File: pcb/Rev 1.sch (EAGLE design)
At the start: 216 parts, among them J1 3220-10-0100-00, J2 10118194-0001LF, J3 B2B-PH-K-S(LF)(SN), Q1 MMBT3904,215MMBT3904,215, Q12 MMBT3904,215MMBT3904,215, Q13 MMBT3904,215MMBT3904,215, Q14 MMBT3904,215MMBT3904,215, Q15 MMBT3904,215MMBT3904,215, Q16 TEFT4300, Q17 TEFT4300, Q18 TEFT4300, Q19 TEFT4300, Q20 MMBT3904,215MMBT3904,215, Q21 MMBT3904,215MMBT3904,215, Q22 MMBT3904,215MMBT3904,215, Q23 MMBT3904,215MMBT3904,215, Q24 TEFT4300, Q25 TEFT4300, Q26 TEFT4300, Q27 TEFT4300, Q28 SI7157DP, Q29 SI7157DP, Q30 MMBT3906, Q31 MMBT3906, Q32 SI7157DP, Q33 MMBT3906, Q34 MMBT3906, U1 ATSAMD21G18A-MU, U10 DRV8871, U11 PCAL6416A, U12 MAX7315, U2 AP3441, U3 TPS61089, U4 BNO055, U5 MCP73811, U7 DRV8871, U8 DRV8871, U9 DRV8871

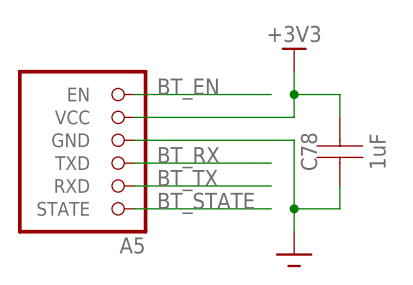
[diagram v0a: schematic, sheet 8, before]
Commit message: Switched power rail to HC-05
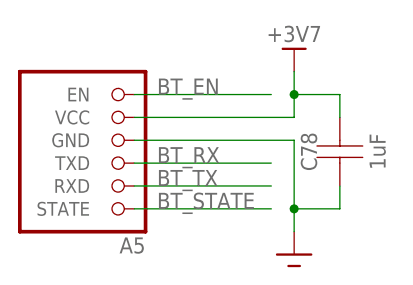
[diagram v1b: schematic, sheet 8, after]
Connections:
- net +3V3: no longer A5.VCC, C78.P$2
- net +3V7: now also A5.VCC, C78.P$2
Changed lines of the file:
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@@
 <part name="GND88" library="Micromouse 2020" deviceset="GND" device=""/>
 <part name="A5" library="Micromouse 2020" deviceset="HC-05" device=""/>
-<part name="P+69" library="Micromouse 2020" deviceset="+3V3" device=""/>
 <part name="GND91" library="Micromouse 2020" deviceset="GND" device=""/>
 <part name="C78" library="Micromouse 2020" deviceset="CAPACITOR" device="0603" package3d_urn="urn:adsk.eagle:package:16053670/1" value="1uF"/>
@@
 <part name="C48" library="Micromouse 2020" deviceset="CAPACITOR" device="0603" package3d_urn="urn:adsk.eagle:package:16053670/1" value="0.1uF"/>
 <part name="GND25" library="Micromouse 2020" deviceset="GND" device=""/>
+<part name="P+21" library="Micromouse 2020" deviceset="+3V7" device=""/>
 </parts>
 <sheets>
@@
 <attribute name="NAME" x="1.27" y="-10.795" size="1.778" layer="95" rot="R180"/>
 </instance>
-<instance part="P+69" gate="G$1" x="17.78" y="10.16" smashed="yes">
-<attribute name="VALUE" x="17.78" y="12.7" size="1.778" layer="96" rot="R180" align="bottom-center"/>
-</instance>
 <instance part="GND91" gate="1" x="17.78" y="-12.7" smashed="yes"/>
 <instance part="C78" gate="G$1" x="22.86" y="-5.08" smashed="yes" rot="R90">
@@
 <attribute name="VALUE" x="27.94" y="-1.27" size="1.778" layer="96" rot="R90" align="bottom-center"/>
 </instance>
+<instance part="P+21" gate="G$1" x="17.78" y="10.16" smashed="yes">
+<attribute name="VALUE" x="17.78" y="12.7" size="1.778" layer="96" rot="R180" align="bottom-center"/>
+</instance>
 </instances>
 <busses>
@@
 </segment>
 </net>
-<net name="+3V3" class="0">
+<net name="+3V7" class="0">
 <segment>
 <pinref part="A5" gate="G$1" pin="VCC"/>
 <wire x1="0" y1="2.54" x2="17.78" y2="2.54" width="0.1524" layer="91"/>
-<pinref part="P+69" gate="G$1" pin="+3V3"/>
 <wire x1="17.78" y1="2.54" x2="17.78" y2="5.08" width="0.1524" layer="91"/>
 <pinref part="C78" gate="G$1" pin="P$2"/>
@@
 <wire x1="22.86" y1="5.08" x2="17.78" y2="5.08" width="0.1524" layer="91"/>
 <junction x="17.78" y="5.08"/>
+<pinref part="P+21" gate="G$1" pin="+3V7"/>
 </segment>
 </net>

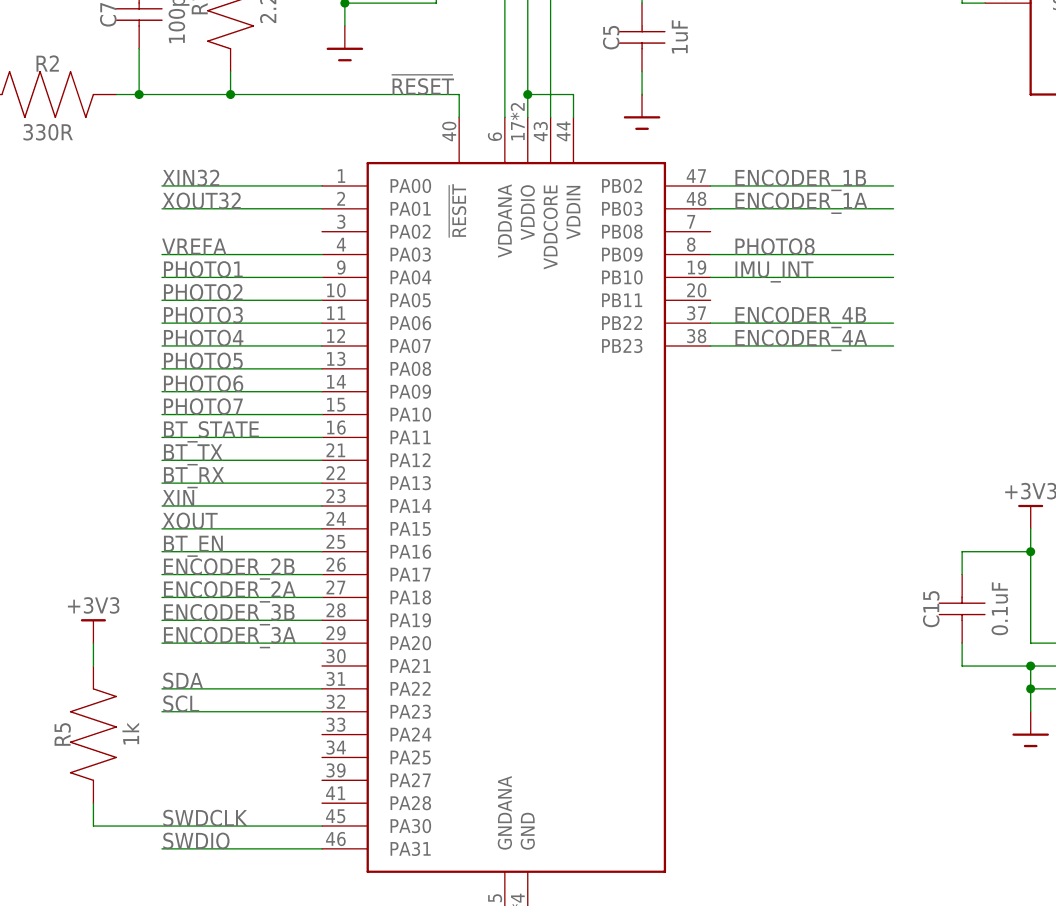
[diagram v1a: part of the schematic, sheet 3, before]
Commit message: Changed pin mapping
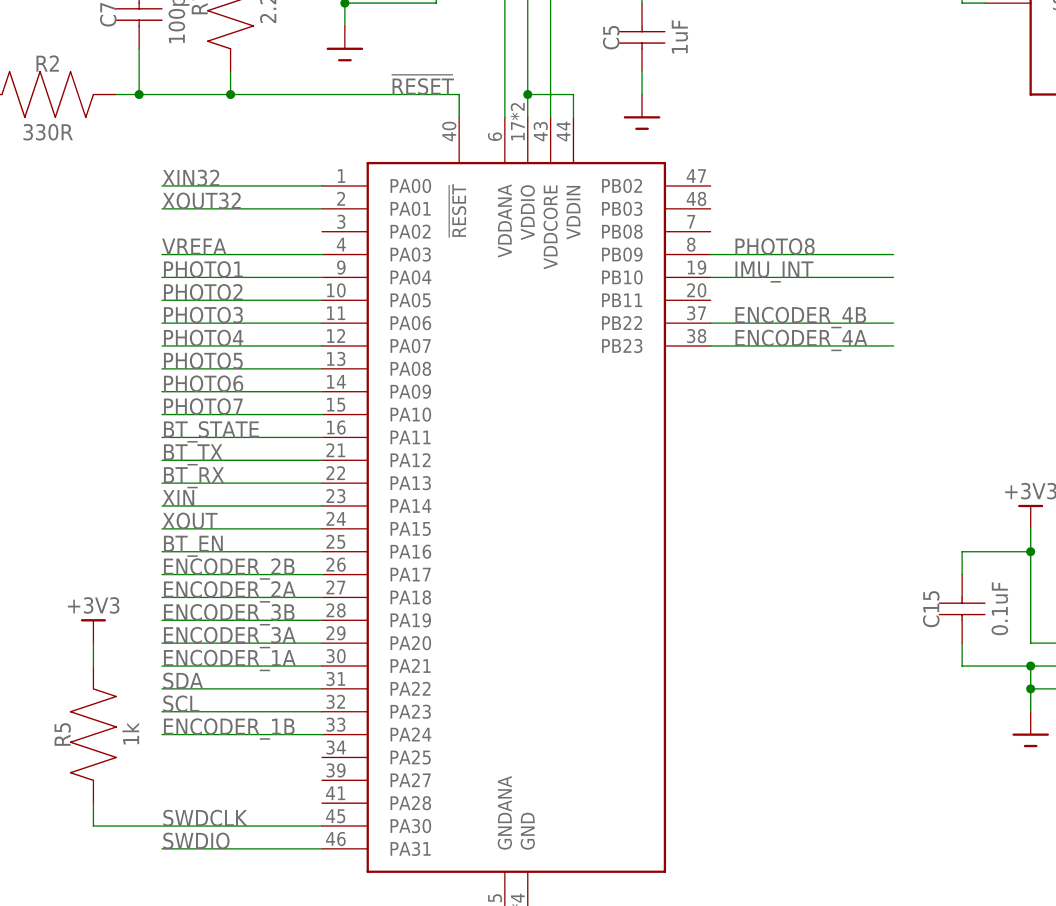
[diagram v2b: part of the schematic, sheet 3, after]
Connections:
- net ENCODER_1A: now also U1.PA21; no longer U1.PB03
- net ENCODER_1B: now also U1.PA24; no longer U1.PB02
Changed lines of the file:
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@@
-</segment>
-</net>
-<net name="ENCODER_1B" class="0">
-<segment>
-<pinref part="U1" gate="G$1" pin="PB02"/>
-<wire x1="20.32" y1="38.1" x2="40.64" y2="38.1" width="0.1524" layer="91"/>
-<label x="22.86" y="38.1" size="1.778" layer="95"/>
 </segment>
 </net>
 <net name="ENCODER_1A" class="0">
 <segment>
-<pinref part="U1" gate="G$1" pin="PB03"/>
-<wire x1="20.32" y1="35.56" x2="40.64" y2="35.56" width="0.1524" layer="91"/>
-<label x="22.86" y="35.56" size="1.778" layer="95"/>
+<pinref part="U1" gate="G$1" pin="PA21"/>
+<wire x1="-22.86" y1="-15.24" x2="-40.64" y2="-15.24" width="0.1524" layer="91"/>
+<label x="-40.64" y="-15.24" size="1.778" layer="95"/>
 </segment>
 </net>
@@
 </segment>
 </net>
+<net name="ENCODER_1B" class="0">
+<segment>
+<pinref part="U1" gate="G$1" pin="PA24"/>
+<wire x1="-22.86" y1="-22.86" x2="-40.64" y2="-22.86" width="0.1524" layer="91"/>
+<label x="-40.64" y="-22.86" size="1.778" layer="95"/>
+</segment>
+</net>
